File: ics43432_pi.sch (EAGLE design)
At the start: 9 parts, among them U1 ICS43432

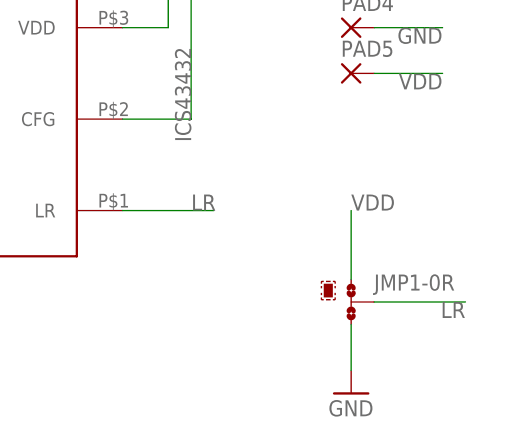
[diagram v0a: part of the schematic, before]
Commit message: added photos of assembled circuits
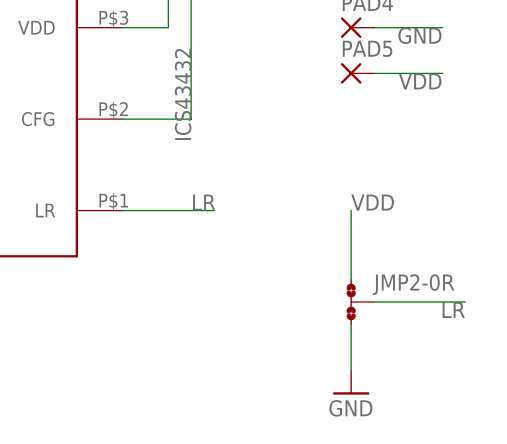
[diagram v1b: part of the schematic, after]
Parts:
- removed JMP1: 0R-JUMPA, jump-0r-smd:0R-JUMPA
- added JMP2: 0R-JUMPC, jump-0r-smd:0R-JUMPC
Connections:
- net GND: now also JMP2-0R.3; no longer JMP1-0R.3
- net LR: now also JMP2-0R.2; no longer JMP1-0R.2
- net VDD: now also JMP2-0R.1; no longer JMP1-0R.1
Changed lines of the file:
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@@
 <part name="PAD4" library="wirepad" deviceset="SMD2" device=""/>
 <part name="PAD5" library="wirepad" deviceset="SMD2" device=""/>
-<part name="JMP1" library="jump-0r-smd" deviceset="0R-JUMP" device="A"/>
 <part name="GND3" library="supply1" deviceset="GND" device=""/>
+<part name="JMP2" library="jump-0r-smd" deviceset="0R-JUMP" device="C"/>
 </parts>
 <sheets>
@@
 <instance part="PAD4" gate="1" x="106.68" y="33.02"/>
 <instance part="PAD5" gate="1" x="106.68" y="27.94"/>
-<instance part="JMP1" gate="-0R" x="106.68" y="2.54"/>
-<instance part="JMP1" gate="G$2" x="104.14" y="5.08"/>
 <instance part="GND3" gate="1" x="106.68" y="-7.62"/>
+<instance part="JMP2" gate="-0R" x="106.68" y="2.54"/>
 </instances>
 <busses>
@@
 <pinref part="GND3" gate="1" pin="GND"/>
 <wire x1="106.68" y1="0" x2="106.68" y2="-5.08" width="0.1524" layer="91"/>
-<pinref part="JMP1" gate="-0R" pin="3"/>
+<pinref part="JMP2" gate="-0R" pin="3"/>
 </segment>
 </net>
@@
 <wire x1="119.38" y1="2.54" x2="109.22" y2="2.54" width="0.1524" layer="91"/>
 <label x="119.38" y="2.54" size="1.778" layer="95" rot="R180"/>
-<pinref part="JMP1" gate="-0R" pin="2"/>
+<pinref part="JMP2" gate="-0R" pin="2"/>
 </segment>
 </net>
@@
 <wire x1="106.68" y1="5.08" x2="106.68" y2="12.7" width="0.1524" layer="91"/>
 <label x="106.68" y="12.7" size="1.778" layer="95"/>
-<pinref part="JMP1" gate="-0R" pin="1"/>
+<pinref part="JMP2" gate="-0R" pin="1"/>
 </segment>
 </net>
